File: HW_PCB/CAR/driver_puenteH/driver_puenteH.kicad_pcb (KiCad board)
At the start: 2 copper layers, 3 parts, among them IC1 TB6612FNG, J3 Puente H, J4 Puente_H2

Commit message: Añadi nuevo proyecto del puente-H
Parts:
- added C1_Driver1: 0.1uF, Capacitor_SMD:C_0805_2012Metric, F.Cu at (140.1, 67.9)
- added C2_driver1: 0.1uF, Capacitor_SMD:C_0805_2012Metric, F.Cu at (135.7, 69.8)
- added C3_driver1: 10uF, Capacitor_SMD:C_0805_2012Metric, F.Cu at (141.3, 84.9)
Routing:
- net /VM: track 0.00 -> 85.9 mm
- net GND: track 0.00 -> 50.3 mm
- net VCC: track 0.00 -> 26.4 mm
- net /PWMA: track 0.00 -> 10.9 mm
- net /AIN2: track 0.00 -> 10.1 mm
- net /B02: track 0.00 -> 9.92 mm
- net /B01: track 0.00 -> 9.91 mm
- net /PWMB: track 0.00 -> 9.84 mm
- net /A01: track 0.00 -> 9.42 mm
- net /A02: track 0.00 -> 9.40 mm
- net /AIN1: track 0.00 -> 9.30 mm
- net /BIN2: track 0.00 -> 9.06 mm
- net /STBY: track 0.00 -> 8.82 mm
- net /BIN1: track 0.00 -> 8.28 mm

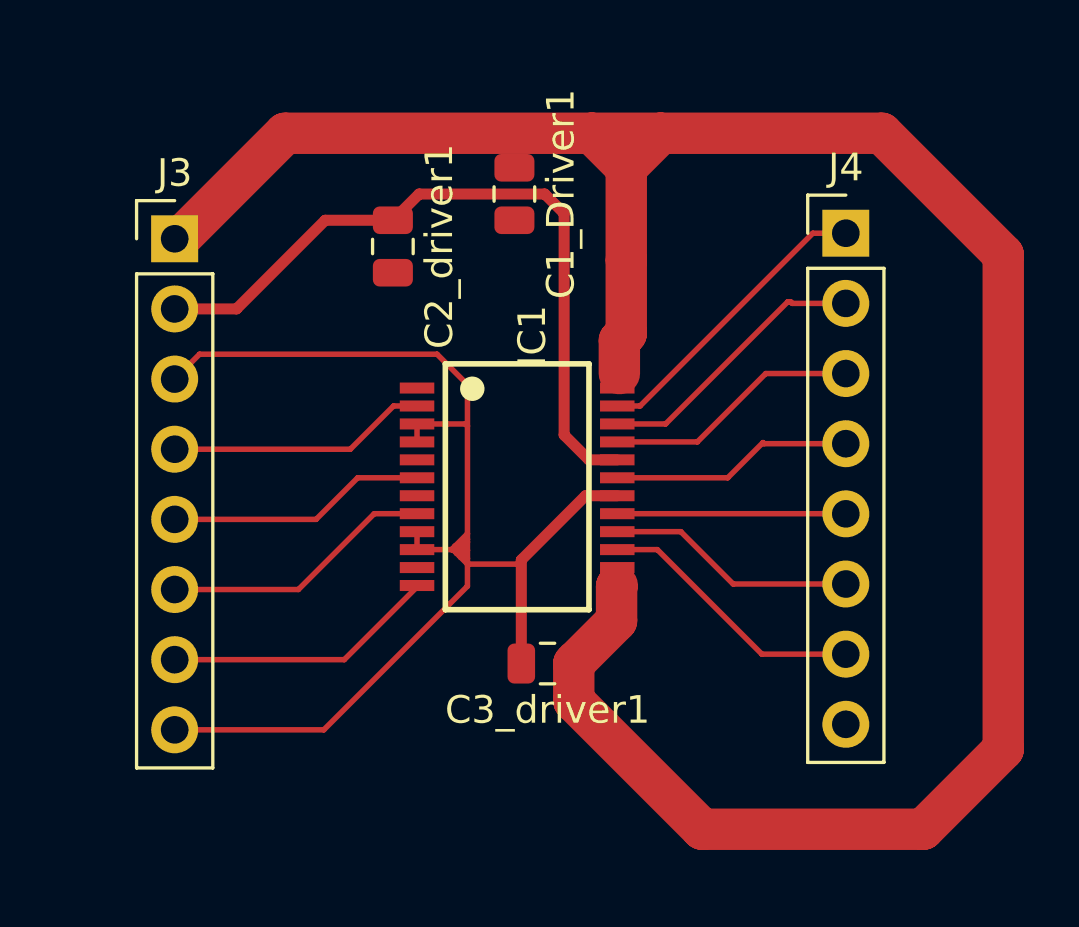
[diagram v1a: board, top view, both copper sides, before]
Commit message: Driver test Finalizado
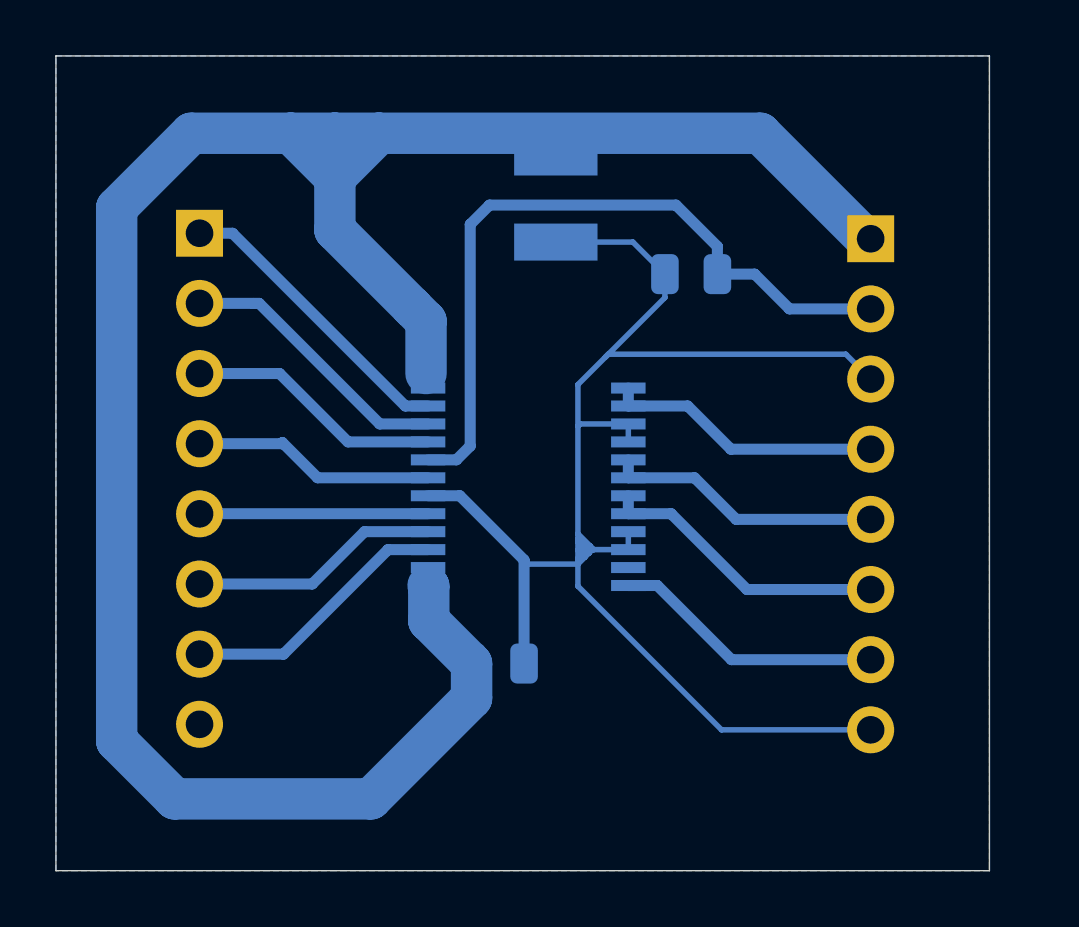
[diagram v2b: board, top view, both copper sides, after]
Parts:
- removed C1_Driver1: 0.1uF, Capacitor_SMD:C_0805_2012Metric
- added C3_Driver1: TAJB226K016RNJ_10uF, TAJB226K016RNJ:CAPPC3528X210N, B.Cu at (141.6, 68.1)
- C2_driver1, C3_driver1, IC1, J3, J4: moved to B.Cu
- moved J3 25.2 mm to (153.0, 69.5), turned to 180 degrees
- moved J4 23.4 mm to (128.7, 69.3), turned to 180 degrees
- moved C2_driver1 10.8 mm to (146.5, 70.8), turned to 180 degrees
- moved C3_driver1 1.80 mm to (139.5, 84.9), turned to 0 degrees
- moved IC1 0.40 mm to (140.6, 78.5)
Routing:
- net GND: track 50.3 -> 58.6 mm
- net /VM: track 85.9 -> 83.9 mm
- net /A01: track 9.42 -> 10.1 mm
- net /A02: track 9.40 -> 10.0 mm
- net /B01: track 9.91 -> 10.6 mm
- added copper zone on B.Cu, net GND
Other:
- board outline added: 33.8 x 29.5 mm

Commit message: Carrito pcb, 25-02-26
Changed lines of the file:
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@@
+	)
+	(segment
+		(start 133.6 69.2)
+		(end 133.6 67.3)
+		(width 1.5)
+		(layer "B.Cu")
+		(net 2)
 	)
 	(segment
@@
 	)
 	(segment
-		(start 136.4 72)
+		(start 136.9 74.4)
 		(end 136.9 72.5)
-		(width 1.5)
-		(layer "B.Cu")
-		(net 2)
-	)
-	(segment
-		(start 133.6 67.3)
-		(end 133.6 69.2)
 		(width 1.5)
 		(layer "B.Cu")
@@
 	)
 	(segment
-		(start 133.6 69.2)
-		(end 136.4 72)
-		(width 1.5)
-		(layer "B.Cu")
-		(net 2)
-	)
-	(segment
 		(start 138.55 84.9)
 		(end 137 83.35)
@@
 	(segment
 		(start 136.9 72.5)
-		(end 136.9 74.4)
+		(end 133.6 69.2)
 		(width 1.5)
 		(layer "B.Cu")

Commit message: Correción menor
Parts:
- C2_driver1, C3_Driver1, C3_driver1, IC1, J3, J4: moved to F.Cu
- moved J3 25.2 mm to (127.8, 69.5), turned to 0 degrees
- moved J4 23.4 mm to (152.1, 69.3), turned to 0 degrees
- moved C2_driver1 12.2 mm to (134.3, 70.8), turned to 0 degrees
- moved C3_Driver1 2.40 mm to (139.2, 68.1)
- moved C3_driver1 1.80 mm to (141.3, 84.9), turned to 180 degrees
- moved IC1 0.40 mm to (140.2, 78.5)
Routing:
- added copper zone on F.Cu, net GND
- removed copper zone on B.Cu, net GND
